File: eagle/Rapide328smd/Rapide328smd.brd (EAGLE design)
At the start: 50 x 50 mm, 32 parts, among them IC1 MEGA8-AI, J1 AVR_SPI_PRG_6PTH

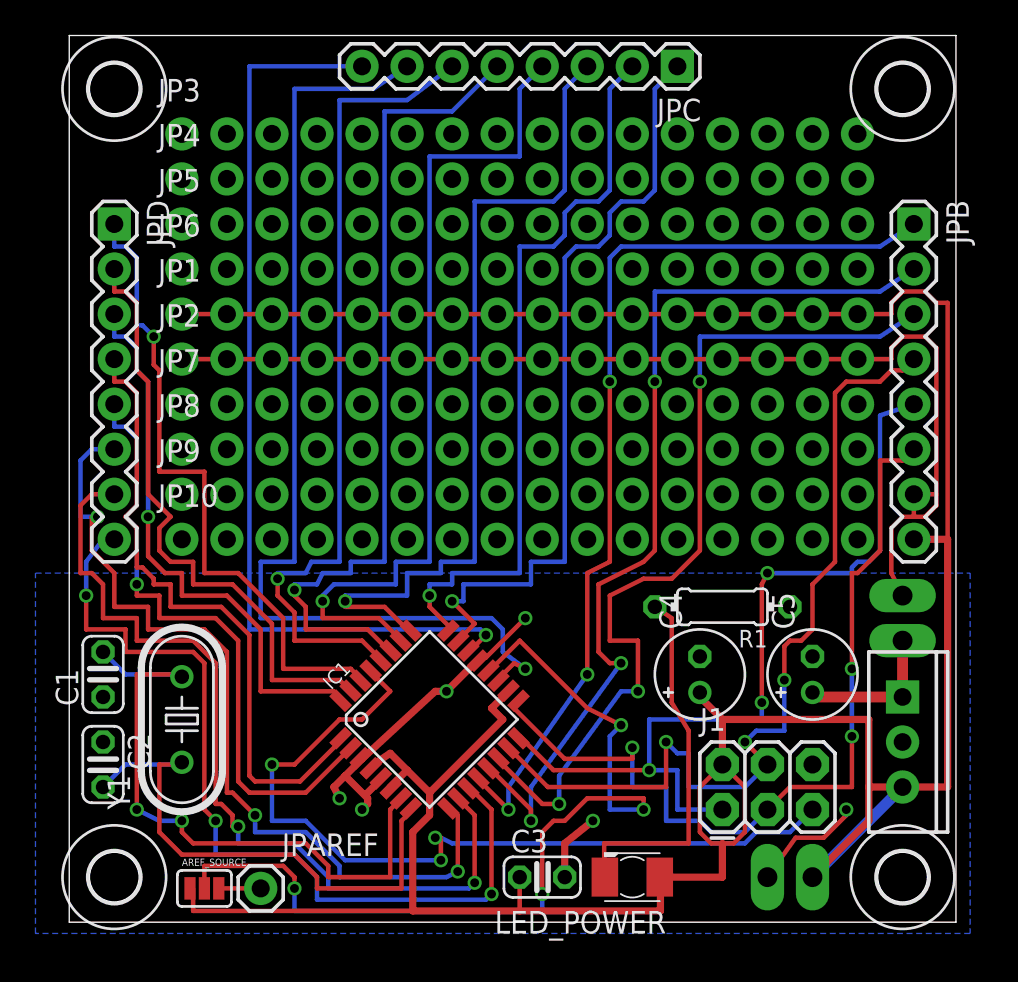
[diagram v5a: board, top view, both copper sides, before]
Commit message: Small modifications : added a useable SMD led on PB5 (SCK), added +/- labels on the back of the board, changed a few wire width.
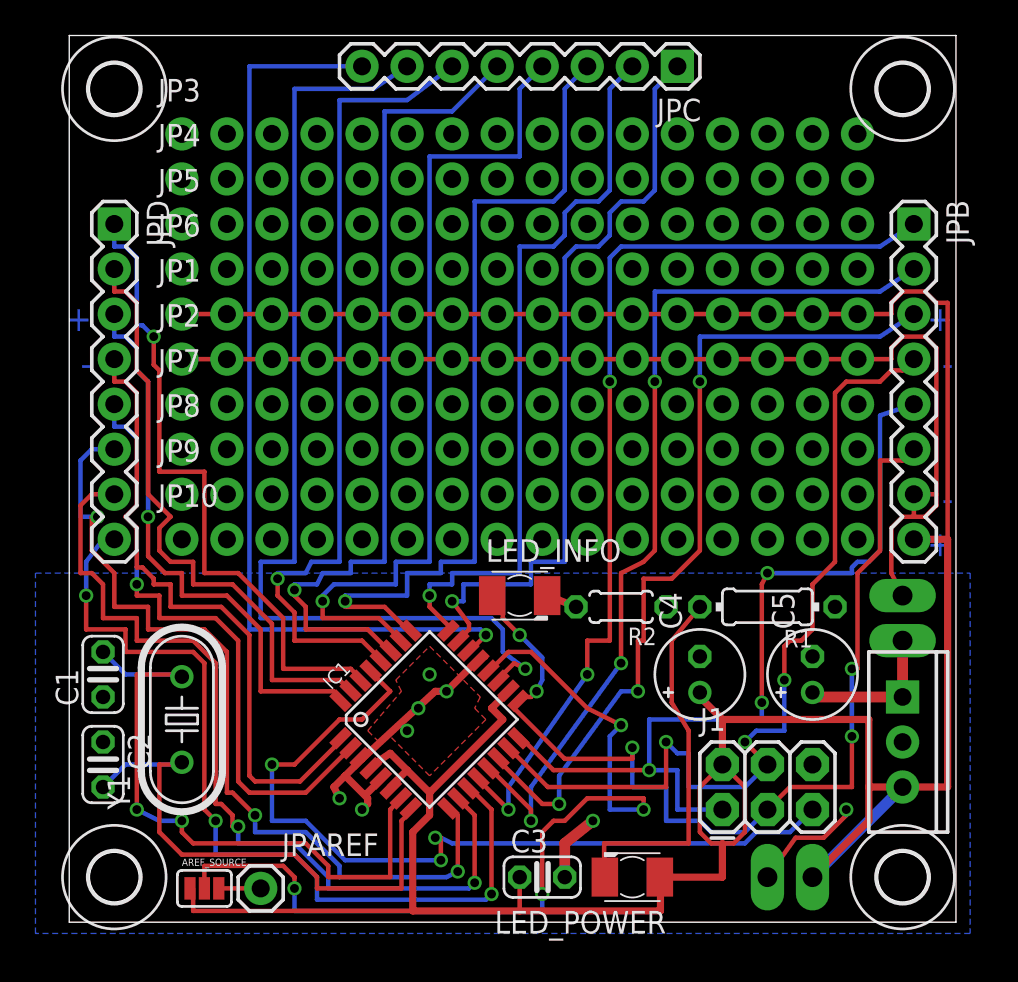
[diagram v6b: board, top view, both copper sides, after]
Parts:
- added LED_INFO: (no value), led:KA-3528ASYC
- added R2: 1k+, resistor:0204/5
- moved R1 2.54 mm to (39.4, 17.8)
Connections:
- new net N$3: LED_INFO.C, R2.2
- net GND: now also R2.1
- net SCK: now also LED_INFO.A
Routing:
- net SCK: track 48.6 -> 56.4 mm, vias 3 -> 5
- net GND: track 92.1 -> 89.0 mm, vias 6 -> 8
- net N$38: track 50.5 -> 48.0 mm
- net N$3: track 0.00 -> 1.71 mm
- net N$34: track 53.4 -> 51.8 mm
- net N$18: track 51.2 -> 50.7 mm
- added copper zone on layer 1, net GND
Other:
- board text added: "B5"
- board text added: "PWR"
- board text added: "Ver 1.0 Jan2013"
- board text removed: "Ver 1.0 Dec2012"
